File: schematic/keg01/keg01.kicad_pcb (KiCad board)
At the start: 2 copper layers, 101.6 x 25.4 mm, 39 parts, among them IC1 ESP-12E, IC2 HX711_SHL, IC3 AP2112K-3.3, P1 Conn_01x03, P2 Conn_01x03, P3 Conn_01x03, P4 Conn_01x03, P5 Conn_01x02, P6 Conn_01x04, X1 NA

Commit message: layout
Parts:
- moved R10 1.91 mm to (117.5, 77.5)
- moved R5 1.90 mm to (108.6, 75.6), turned to 180 degrees
- moved C12 1.27 mm to (141.0, 85.7)
- moved C13 1.27 mm to (140.3, 89.5)
- moved C15 1.27 mm to (134.0, 78.1)
- moved C3 1.27 mm to (120.7, 95.2)
- moved C5 1.27 mm to (134.0, 94.6)
- moved C6 1.27 mm to (139.1, 94.0)
- moved C7 1.27 mm to (136.5, 94.0)
- moved C9 1.27 mm to (127.6, 94.6), turned to 270 degrees
- moved FB1 1.27 mm to (120.7, 92.7)
- moved FB2 1.27 mm to (138.4, 85.7)
- moved H1 1.27 mm to (130.2, 85.7)
- moved IC2 1.27 mm to (158.8, 85.7)
- moved IC3 1.27 mm to (130.8, 94.6)
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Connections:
- net Net-(C12-Pad1) renamed /PWIC2
- net Net-(C5-Pad1) renamed /PWIN2
- net Net-(D1-Pad2) renamed /PWIN
- C16 pad 1: Net-(C16-Pad1) -> /PWDISP
- C17 pad 1: Net-(C16-Pad1) -> /PWDISP
- C3 pad 1: Net-(C3-Pad1) -> /PWIC1
- C4 pad 1: Net-(C3-Pad1) -> /PWIC1
- FB1 pad 1: Net-(C3-Pad1) -> /PWIC1
- FB3 pad 1: Net-(C16-Pad1) -> /PWDISP
- IC1 pad 8: Net-(C3-Pad1) -> /PWIC1
- P6 pad 2: Net-(C16-Pad1) -> /PWDISP
- R1 pad 1: +3V3 -> Net-(IC1-Pad3)
- R1 pad 2: Net-(IC1-Pad3) -> /PWIC1
- R5 pad 1: +3V3 -> /PWDISP
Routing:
- net GND: track 0.00 -> 154.9 mm, vias 0 -> 29
- net /PWIN: track 0.00 -> 61.0 mm, vias 0 -> 2
- net +3V3: track 0.00 -> 47.4 mm
- net LOADCELL_DOUT: track 0.00 -> 47.2 mm, vias 0 -> 2
- net LOADCELL_SCK: track 0.00 -> 44.6 mm, vias 0 -> 2
- net RST: track 0.00 -> 37.1 mm, vias 0 -> 1
- net /PWDISP: track 0.00 -> 30.2 mm, vias 0 -> 2
- net GPIO0: track 0.00 -> 28.7 mm, vias 0 -> 1
- net TXD: track 0.00 -> 24.6 mm, vias 0 -> 1
- net RXD: track 0.00 -> 22.2 mm, vias 0 -> 1
- net /PWIC1: track 0.00 -> 21.8 mm
- net DISP_SDA: track 0.00 -> 21.2 mm, vias 0 -> 2
- net DISP_SCL: track 0.00 -> 20.8 mm, vias 0 -> 2
- net /PWIN2: track 0.00 -> 17.0 mm
- net Net-(IC2-Pad4): track 0.00 -> 15.4 mm
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- added copper zone on B.Cu, net GND
- added copper zone on F.Cu, net GND
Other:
- net class Default: trace_width 0.25 -> 0.4
- net class GND added: clearance 0.3, trace_width 0.6, via_dia 0.8, via_drill 0.4
- net class PWR added: clearance 0.2, trace_width 0.6, via_dia 0.8, via_drill 0.4
- board text added: "+"
- board text added: "-"
- board text added: "B"
- board text added: "GND"
- board text added: "GND 3V3"
- board text added: "GPIO0"
- board text added: "KEG 01"
- board text added: "OH 2101"
- board text added: "R"
- board text added: "RST"
- board text added: "RX TX"
- board text added: "S1"
- board text added: "S2"
- board text added: "S3"
- board text added: "S4"
- board text added: "SCK"
- board text added: "SDA"
- board text added: "VCC"
- board text added: "W"

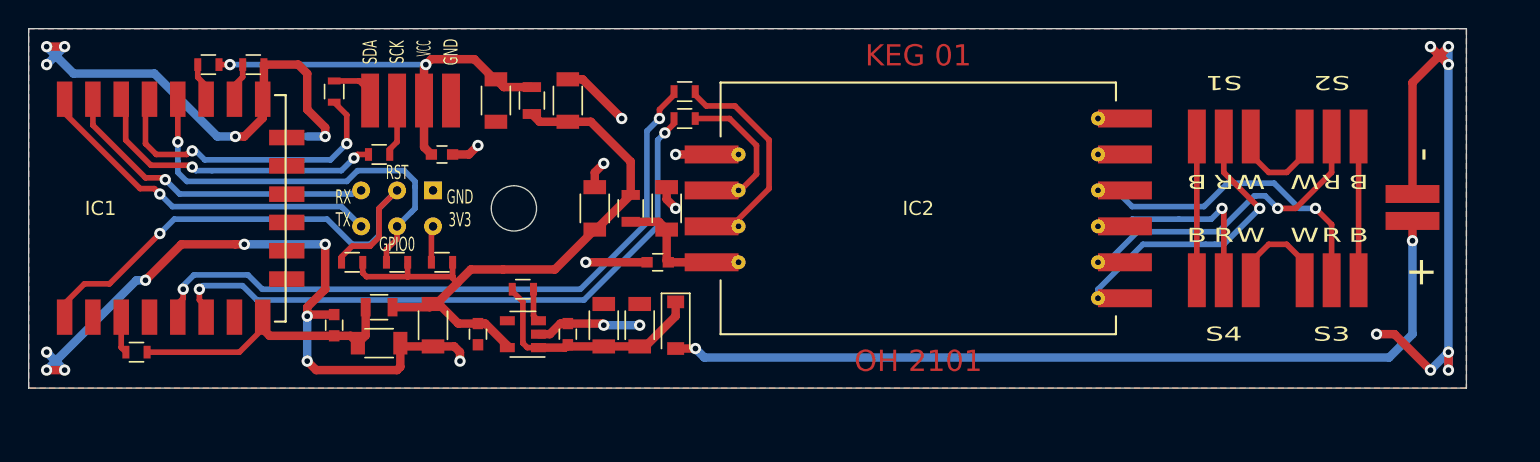
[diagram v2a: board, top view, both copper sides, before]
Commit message: panelizing markers and adjustment
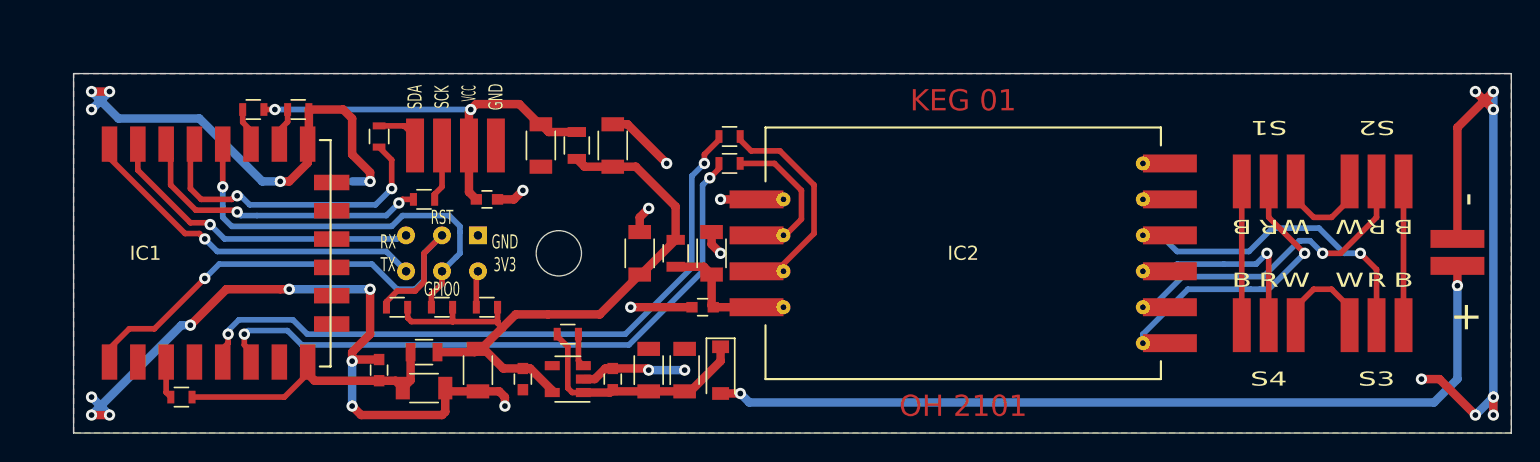
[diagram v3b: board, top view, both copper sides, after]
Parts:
- moved C11 4.49 mm to (139.1, 88.9)
- moved C12 4.49 mm to (144.1, 88.9)
- moved IC2 4.49 mm to (161.9, 88.9)
- moved IC3 4.49 mm to (134.0, 97.8)
- moved C16 4.49 mm to (132.1, 81.3)
- moved C17 4.49 mm to (128.3, 85.1)
- moved C2 4.49 mm to (127.6, 97.2)
- moved C4 4.49 mm to (120.7, 97.2)
- moved C6 4.49 mm to (142.2, 97.2)
- moved C9 4.49 mm to (130.8, 97.8)
- moved D1 4.49 mm to (144.8, 97.2)
- moved FB1 4.49 mm to (123.8, 95.9)
- moved FB3 4.49 mm to (134.6, 81.3)
- moved IC1 4.49 mm to (101.6, 95.9)
- moved R1 4.49 mm to (106.7, 99.1)
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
